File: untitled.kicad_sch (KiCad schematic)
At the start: 0 parts

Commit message: routed power
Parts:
- added C17, C18: C_00005, symbol mic_patch_parts:C_00005
- added C19: C_00006, symbol mic_patch_parts:C_00006
- added C20: C_00003, symbol mic_patch_parts:C_00003
- added D1: LED_0001, symbol mic_patch_parts:LED_0001
- added D2: LED_0002, symbol mic_patch_parts:LED_0002
- added J2, J3: J_000001, symbol mic_patch_parts:J_000001
- added L3: L_00002, symbol mic_patch_parts:L_00002
- added R2: R_00002, symbol mic_patch_parts:R_00002
- added R3, R4, R5: R_00002, symbol mic_patch_parts:R_00003
- added U2: PWR_nPM1100-QDXX, Package_DFN_QFN:QFN-24-1EP_4x4mm_P0.5mm_EP2.6x2.6mm_ThermalVias, symbol mic_patch_parts:PWR_nPM1100-QDXX
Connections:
- new net: R3.2, U2.14 (NTC)
- new net: L3.2, U2.22 (SW)
- new net: D1.2 (A), R5.2
- new net: R2.2, U2.12 (ICHG)
- new net: C20.1, J3.2, U2.15 (VBAT)
- new net: C18.1, U2.21 (DEC)
- new net: D2.2 (A), R4.2
- new net: D2.1 (K), U2.10 (ERR)
- new net: C19.1, J2.1, U2.17 (VBUS)
- new net: D1.1 (K), U2.8 (CHG)
- new net +1V8 VDD_NRF: C17.1, L3.1, U2.1 (VOUTB), U2.7 (MODE)
- new net GND: C17.2, C18.2, C19.2, C20.2, J2.2, J3.1, R2.1, R3.1, U2.11 (SHPHLD), U2.19 (D-), U2.2 (VOUTBSET1), U2.23 (PVSS), U2.25 (AVSS), U2.3 (VOUTBSET0), U2.4 (AVSS), U2.5 (ISET), U2.6 (SHPACT)
- new net VSYS: R4.1, R5.1, U2.16 (VSYS), U2.9 (VTERMSET)
- no-connect marks 0 -> 1
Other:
- note added: "AVSS for fixed 100ma"
- note added: "Avss for fixed 100ma - no negotiation"
- note added: "Battery"
- note added: "Could connect these straight to the MCU....."
- note added: "Pull mode high for foce PWM"
- note added: "Set VDD to 1.8V"
- note added: "Star point meet between RFGND & PVSS. Pour under Pmic pad then add vias to RF GND plane + main GND"
- note added: "Test point here"
- note added: "V In"

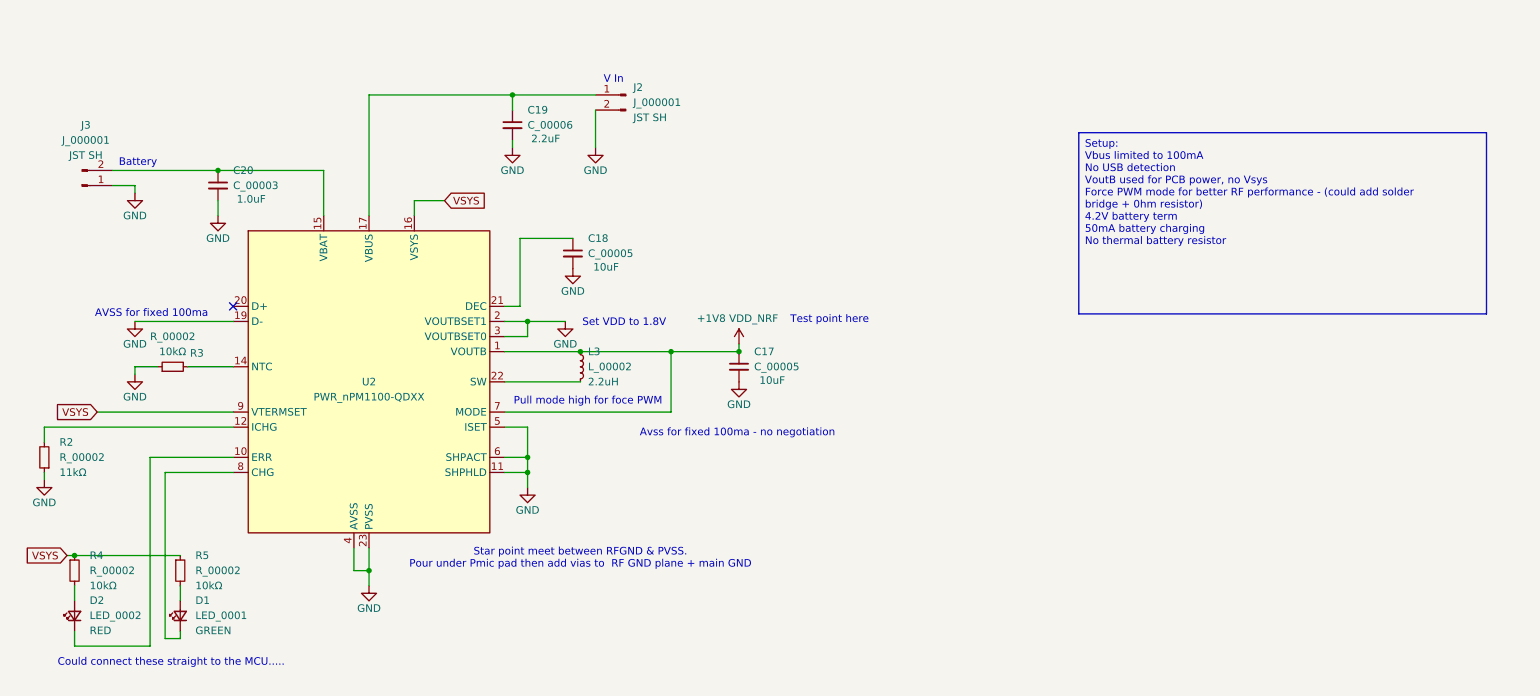
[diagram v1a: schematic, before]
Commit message: added in LFCLK
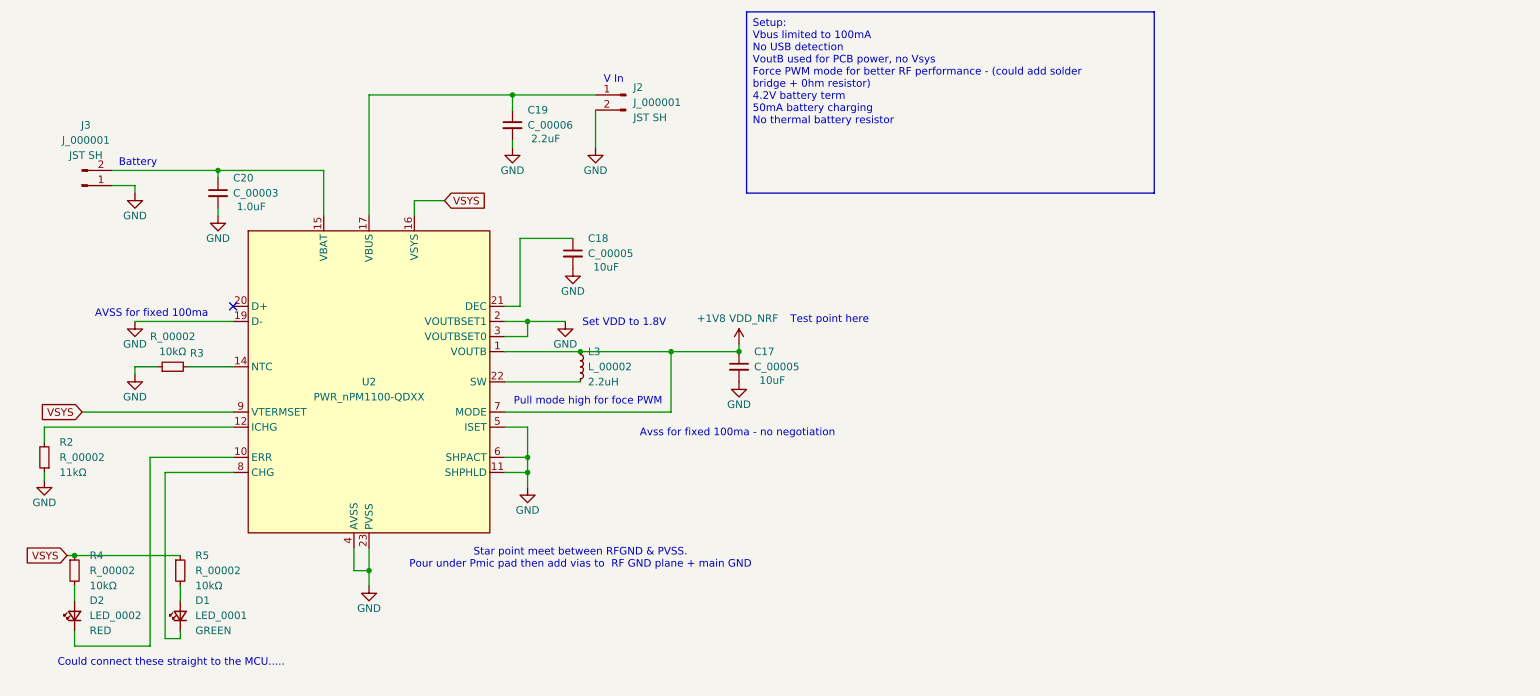
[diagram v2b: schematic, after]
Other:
- moved on the sheet: C20
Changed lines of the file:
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@@
+	(wire
+		(pts
+			(xy 45.72 45.72) (xy 45.72 44.45)
+		)
+		(stroke
+			(width 0)
+			(type default)
+		)
+	)
 	(wire
 		(pts
@@
 	(wire
 		(pts
-			(xy 45.72 52.07) (xy 45.72 49.53)
+			(xy 45.72 52.07) (xy 45.72 50.8)
 		)
 		(stroke
@@
 	(wire
 		(pts
-			(xy 25.4 85.09) (xy 48.26 85.09)
+			(xy 22.86 85.09) (xy 48.26 85.09)
 		)
 		(stroke
@@
 	(text_box "Setup:\nVbus limited to 100mA\nNo USB detection\nVoutB used for PCB power, no Vsys\nForce PWM mode for better RF performance - (could add solder bridge + 0hm resistor)\n4.2V battery term\n50mA battery charging\nNo thermal battery resistor\n\n"
 		(exclude_from_sim no)
-		(at 190.5 38.1 0)
+		(at 134.62 17.78 0)
 		(size 68.58 30.48)
 		(stroke
@@
 	(global_label "VSYS"
 		(shape input)
-		(at 25.4 85.09 180)
+		(at 22.86 85.09 180)
 		(fields_autoplaced yes)
 		(effects
@@
 		)
 		(property "Intersheetrefs" "${INTERSHEET_REFS}"
-			(at 17.8186 85.09 0)
+			(at 15.2786 85.09 0)
 			(effects
 				(font
@@
 	(symbol
 		(lib_id "mic_patch_parts:C_00003")
-		(at 45.72 46.99 0)
+		(at 45.72 48.26 0)
 		(unit 1)
 		(exclude_from_sim no)
@@
 		(fields_autoplaced yes)
 		(property "Reference" "C20"
-			(at 48.26 44.45 0)
+			(at 48.26 45.72 0)
 			(do_not_autoplace yes)
 			(effects
@@
 		)
 		(property "Value" "C_00003"
-			(at 48.26 46.99 0)
+			(at 48.26 48.26 0)
 			(do_not_autoplace yes)
 			(effects
@@
 		)
 		(property "Footprint" ""
-			(at 20.32 48.26 0)
+			(at 20.32 49.53 0)
 			(effects
 				(font
@@
 		)
 		(property "Datasheet" "~"
-			(at 45.72 46.99 0)
+			(at 45.72 48.26 0)
 			(effects
 				(font
@@
 		)
 		(property "Description" "1.0uF"
-			(at 51.308 49.276 0)
+			(at 51.308 50.546 0)
 			(do_not_autoplace yes)
 			(effects
@@
 		)
 		(property "Desc" ""
-			(at 48.26 49.53 0)
+			(at 48.26 50.8 0)
 			(do_not_autoplace yes)
 			(effects
@@
 		)
 		(property "MPNs" ""
-			(at 24.13 39.37 0)
+			(at 24.13 40.64 0)
 			(effects
 				(font
@@
 		)
 		(property "LCSC PNs" ""
-			(at 25.4 44.45 0)
-			(effects
-				(font
+			(at 25.4 45.72 0)
+			(effects
+				(font

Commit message: added ADAU7002 Symbol
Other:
- note added: "50mA charge"
- note added: "V In - USB?"
- note removed: "V In"
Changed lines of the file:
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@@
 	(wire
 		(pts
-			(xy 34.29 92.71) (xy 34.29 124.46)
+			(xy 34.29 92.71) (xy 34.29 123.19)
 		)
 		(stroke
@@
 	(wire
 		(pts
-			(xy 21.59 121.92) (xy 21.59 124.46)
+			(xy 21.59 121.92) (xy 21.59 123.19)
 		)
 		(stroke
@@
 	(wire
 		(pts
-			(xy 21.59 124.46) (xy 34.29 124.46)
+			(xy 21.59 123.19) (xy 34.29 123.19)
 		)
 		(stroke
@@
 		)
 	)
-	(text "V In"
-		(exclude_from_sim no)
-		(at 112.268 29.21 0)
+	(text "V In - USB?"
+		(exclude_from_sim no)
+		(at 112.268 28.194 0)
 		(effects
 			(font
@@
 		(effects
 			(font
+				(size 1.27 1.27)
+			)
+		)
+	)
+	(text "50mA charge"
+		(exclude_from_sim no)
+		(at 26.67 98.806 0)
+		(effects
+			(font

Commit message: added rudimentary RF matching network
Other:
- note added: "Bulk Decoupling"
- moved on the sheet: C17, C18, C19, C20, D1, D2, J2, J3, L3, R2, R3, R4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

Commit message: updated power supply to 3.0V to support micro SD card
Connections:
- net GND: no longer U2.2 (VOUTBSET1), U2.3 (VOUTBSET0)
- net VSYS: now also U2.2 (VOUTBSET1), U2.3 (VOUTBSET0)
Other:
- note added: "Change VDD to 3.3V"
- note added: "Set VDD to 3.0V"
- note removed: "Set VDD to 1.8V"
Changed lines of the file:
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@@
+	(wire
+		(pts
+			(xy 152.4 69.85) (xy 152.4 72.39)
+		)
+		(stroke
+			(width 0)
+			(type default)
+		)
+	)
 	(wire
 		(pts
@@
 	(wire
 		(pts
+			(xy 152.4 69.85) (xy 154.94 69.85)
+		)
+		(stroke
+			(width 0)
+			(type default)
+		)
+	)
+	(wire
+		(pts
 			(xy 88.9 95.25) (xy 102.87 95.25)
 		)
@@
 		(pts
 			(xy 76.2 111.76) (xy 93.98 111.76)
-		)
-		(stroke
-			(width 0)
-			(type default)
-		)
-	)
-	(wire
-		(pts
-			(xy 152.4 72.39) (xy 158.75 72.39)
 		)
 		(stroke
@@
 		)
 	)
-	(text "Set VDD to 1.8V"
-		(exclude_from_sim no)
-		(at 168.656 72.644 0)
+	(text "Change VDD to 3.3V"
+		(exclude_from_sim no)
+		(at 181.356 64.008 0)
+		(effects
+			(font
+				(size 1.27 1.27)
+			)
+		)
+	)
+	(text "Set VDD to 3.0V"
+		(exclude_from_sim no)
+		(at 165.1 72.644 0)
 		(effects
 			(font
@@
 			(font
 				(size 1.27 1.27)
+			)
+		)
+	)
+	(global_label "VSYS"
+		(shape input)
+		(at 154.94 69.85 0)
+		(fields_autoplaced yes)
+		(effects
+			(font
+				(size 1.27 1.27)
+			)
+			(justify left)
+		)
+		(property "Intersheetrefs" "${INTERSHEET_REFS}"
+			(at 162.5214 69.85 0)
+			(effects
+				(font
+					(size 1.27 1.27)
+				)
+				(justify left)
+				(hide yes)
 			)
 		)
@@
 					(unit 1)
 				)
-			)
-		)
-	)
-	(symbol
-		(lib_id "power:GND")
-		(at 158.75 72.39 0)
-		(unit 1)
-		(exclude_from_sim no)
-		(in_bom yes)
-		(on_board yes)
-		(dnp no)
-		(property "Reference" "#PWR023"
-			(at 158.75 78.74 0)
-			(effects
-				(font
-					(size 1.27 1.27)
-				)
-				(hide yes)
-			)
-		)
-		(property "Value" "GND"
-			(at 158.75 76.2 0)
-			(effects
-				(font
-					(size 1.27 1.27)
-				)
-			)
-		)
-		(property "Footprint" ""
-			(at 158.75 72.39 0)
-			(effects
-				(font
-					(size 1.27 1.27)
-				)
-				(hide yes)
-			)
-		)
-		(property "Datasheet" ""
-			(at 158.75 72.39 0)
-			(effects
-				(font
-					(size 1.27 1.27)
-				)
-				(hide yes)
-			)
-		)
-		(property "Description" "Power symbol creates a global label with name \"GND\" , ground"
-			(at 158.75 72.39 0)
-			(effects
-				(font
-					(size 1.27 1.27)
-				)
-				(hide yes)
-			)
-		)
-		(pin "1"
-		)
-		(instances
-			(project "mic_patch_v1"
-				(path "/5448a297-4261-40a5-8009-47199bfe22cb/549bd3f0-5402-4113-b11d-8a88b4fc0730"
-					(reference "#PWR023")
-					(unit 1)
-				)

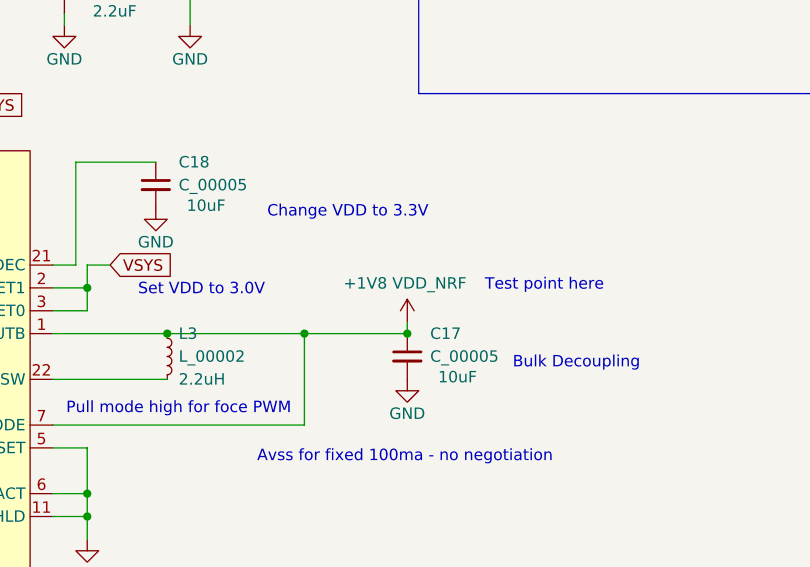
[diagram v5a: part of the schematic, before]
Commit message: routed pins for SD card
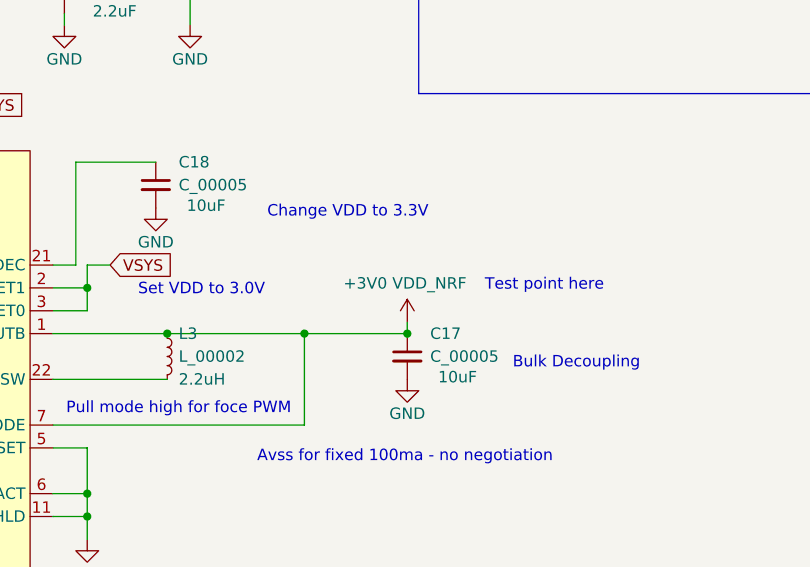
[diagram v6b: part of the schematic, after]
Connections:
- net +1V8 VDD_NRF renamed +3V0 VDD_NRF
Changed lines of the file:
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@@
 			)
 		)
-		(property "Value" "+1V8 VDD_NRF"
+		(property "Value" "+3V0 VDD_NRF"
 			(at 187.706 71.882 0)
 			(effects

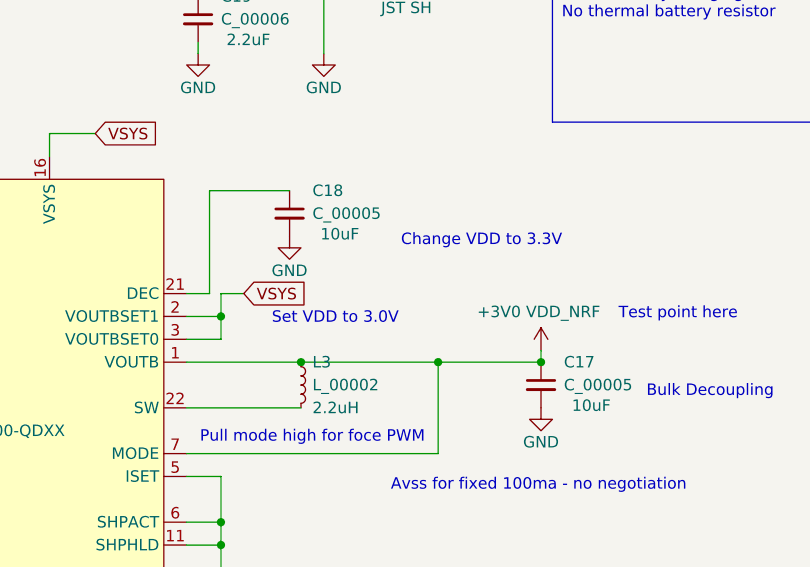
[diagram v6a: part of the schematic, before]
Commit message: added two active high push buttons
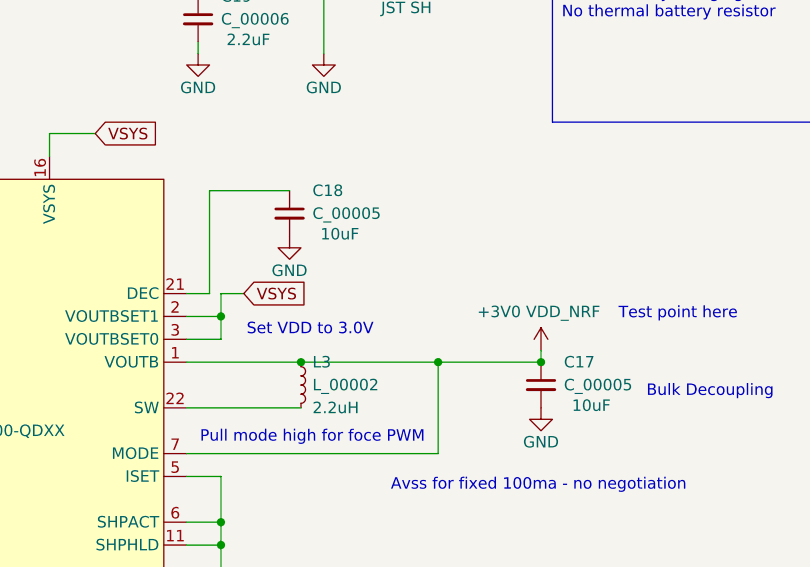
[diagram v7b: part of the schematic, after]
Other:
- note removed: "Change VDD to 3.3V"
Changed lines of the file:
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@@
-		)
-	)
-	(text "Change VDD to 3.3V"
-		(exclude_from_sim no)
-		(at 181.356 64.008 0)
-		(effects
-			(font
-				(size 1.27 1.27)
-			)
 		)
 	)
 	(text "Set VDD to 3.0V"
 		(exclude_from_sim no)
-		(at 165.1 72.644 0)
+		(at 162.306 73.914 0)
 		(effects
 			(font

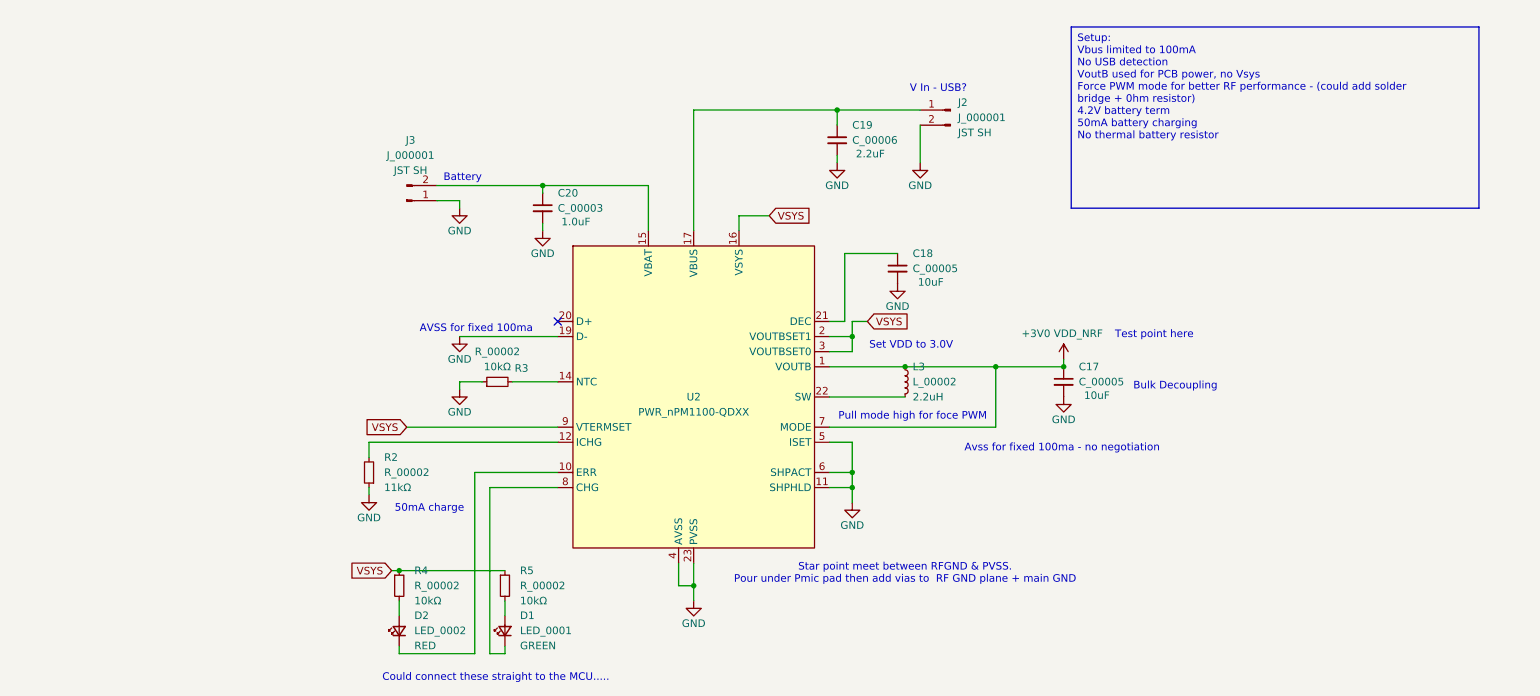
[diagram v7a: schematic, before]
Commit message: changed vterm to 4.25V on the npm1100, added GPIO control of npm1100 BUCK modes
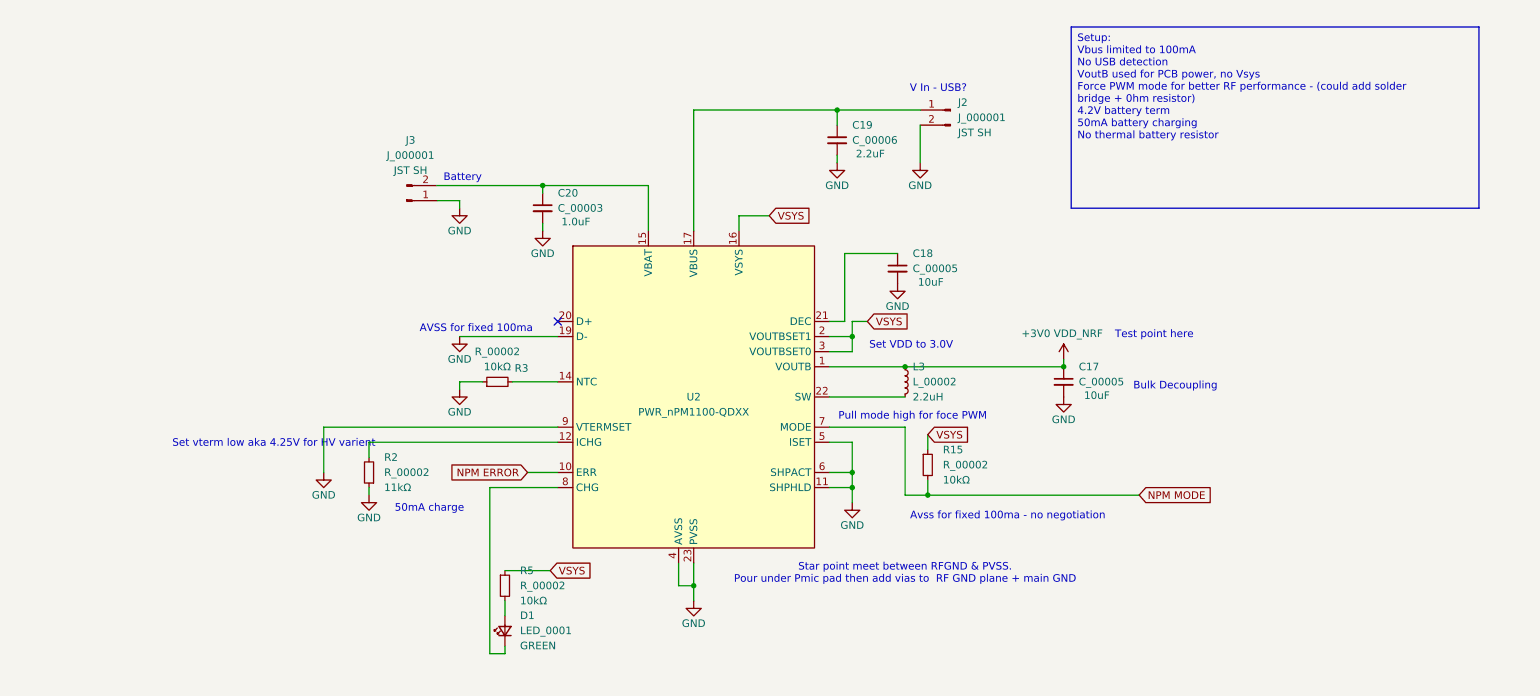
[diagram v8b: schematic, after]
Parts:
- removed D2: LED_0002, symbol mic_patch_parts:LED_0002
- removed R4: R_00002, symbol mic_patch_parts:R_00003
- added R15: R_00002, symbol mic_patch_parts:R_00003
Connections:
- net +3V0 VDD_NRF: no longer U2.7 (MODE)
- net GND: now also U2.9 (VTERMSET)
- net VSYS: now also R15.1; no longer U2.9 (VTERMSET)
- net NPM ERROR: now reaches U2.10 (ERR)
- new net NPM MODE: R15.2, U2.7 (MODE)
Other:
- note added: "Set vterm low aka 4.25V for HV varient"
- note removed: "Could connect these straight to the MCU....."
